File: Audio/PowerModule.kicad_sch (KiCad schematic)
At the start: 15 parts, among them J4 PWR_IN, J5 PWR_OUT, U1 TMR 6-1223

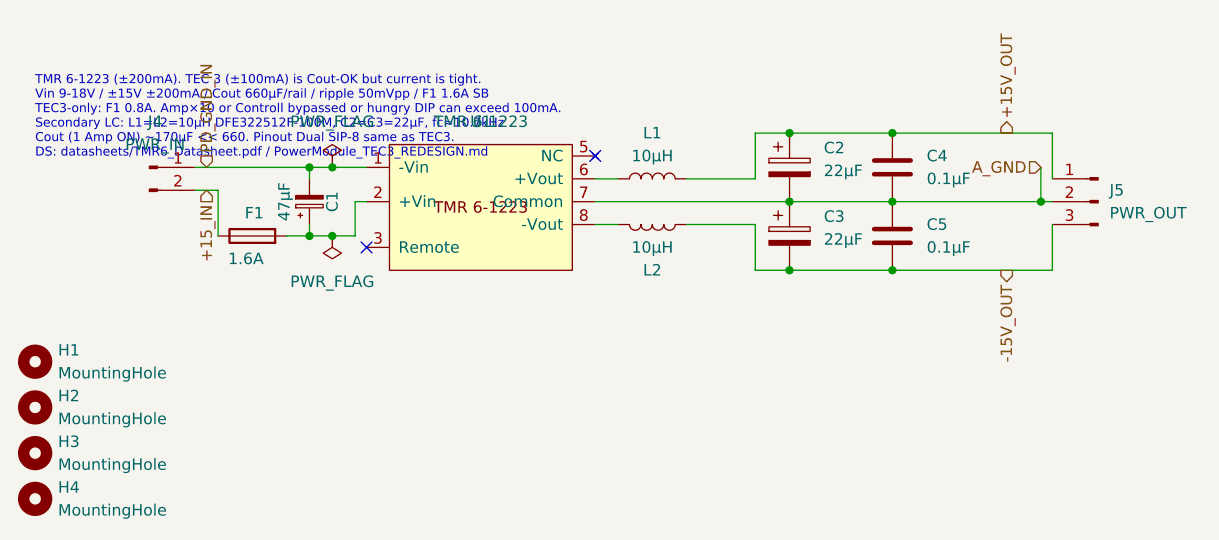
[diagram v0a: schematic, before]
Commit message: PowerModule の U1 を MEAN WELL DKMW20F-15 にする。
SIP-8 の TMR 6 では Amp 複数同時の電流が足りない。1インチ Dual に載せ替え、
ヒューズを 3A delay にし、ピン配置は SIP と別物としてシンボルと FP を新設する。

Co-authored-by: m_arino <indare@users.noreply.github.com>
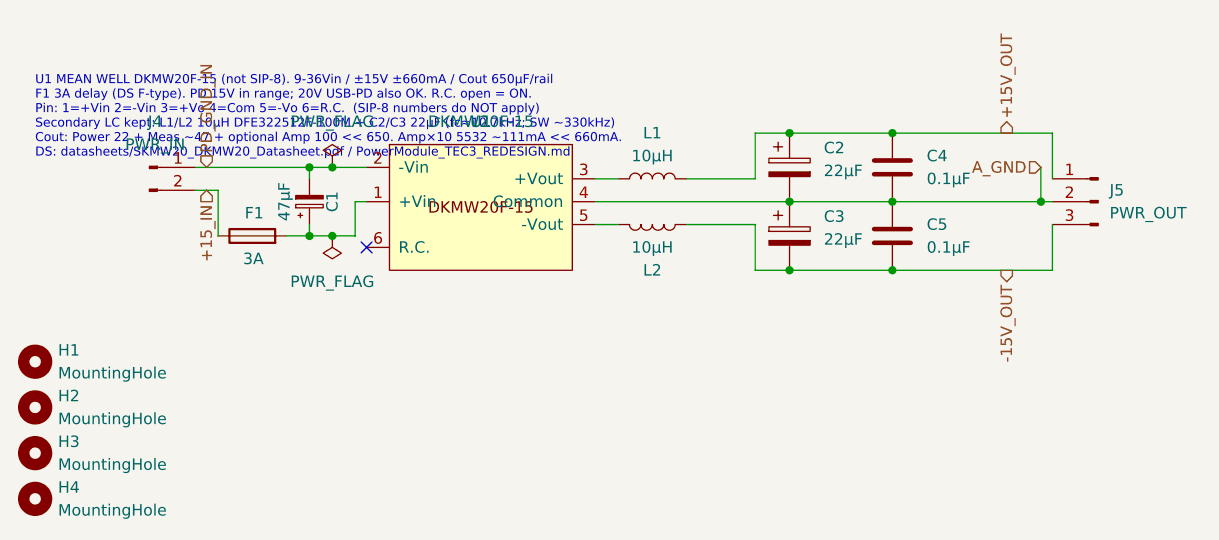
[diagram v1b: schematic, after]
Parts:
- F1: value 1.6A -> 3A
- U1: value TMR 6-1223 -> DKMW20F-15; footprint Library:TEC3-1223_SIP8_THT -> Library:DKMW20F-15_1in_THT; symbol TEC3:TEC3-1223 -> DKMW20:DKMW20F-15; MPN TMR 6-1223 -> DKMW20F-15; Manufacturer Traco Power -> MEAN WELL
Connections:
- net A_GND: now also U1.4 (Common); no longer U1.7 (Common)
- net PD_GND_IN: now also U1.2 (-Vin); no longer U1.1 (-Vin)
- net at L1.2: now also U1.3 (+Vout); no longer U1.6 (+Vout)
- net at C1.1, F1.2: now also U1.1 (+Vin); no longer U1.2 (+Vin)
- net at U1.5 (-Vout): now also L2.1
- no-connect marks 2 -> 1
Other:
- note added: "U1 MEAN WELL DKMW20F-15 (not SIP-8). 9-36Vin / ±15V ±660mA / Cout 650µF/rail F1 3A delay (DS F-type). PD 15V in range; 20V USB-PD also OK. R.C. open = ON. Pin: 1=+Vin 2=-Vin 3=+Vo 4=Com 5=-Vo 6=R.C. (SIP-8 numbers do NOT apply) Secondary LC kept: L1/L2 10µH DFE322512F-100M + C2/C3 22µF (fc≈10.7kHz; SW ~330kHz) Cout: Power 22 + Meas ~47 + optional Amp 100 << 650. Amp×10 5532 ~111mA << 660mA. DS: d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"
- note removed: "TMR 6-1223 (±200mA). TEC 3 (±100mA) is Cout-OK but current is tight. Vin 9-18V / ±15V ±200mA / Cout 660µF/rail / ripple 50mVpp / F1 1.6A SB TEC3-only: F1 0.8A. Amp×10 or Controll bypassed or hungry DIP can exceed 100mA. Secondary LC: L1=L2=10µH DFE322512F-100M, C2=C3=22µF, fc≈10.7kHz Cout (1 Amp ON) ~170µF << 660. Pinout Dual SIP-8 same as TEC3. DS: datasheets/TMR6_Datasheet.pdf / PowerModule_TEC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"
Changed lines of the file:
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@@
-	)
-	(no_connect
-		(at 77.47 35.56)
-		(uuid "b0a0tec3-0002-4000-8000-000000000002")
 	)
 	(no_connect
@@
 		)
 	)
-	(text "TMR 6-1223 (±200mA). TEC 3 (±100mA) is Cout-OK but current is tight.\nVin 9-18V / ±15V ±200mA / Cout 660µF/rail / ripple 50mVpp / F1 1.6A SB\nTEC3-only: F1 0.8A. Amp×10 or Controll bypassed or hungry DIP can exceed 100mA.\nSecondary LC: L1=L2=10µH DFE322512F-100M, C2=C3=22µF, fc≈10.7kHz\nCout (1 Amp ON) ~170µF << 660. Pinout Dual SIP-8 same as TEC3.\nDS: datasheets/TMR6_Datasheet.pdf / PowerModule_TEC3_REDESIGN.md"
+	(text "U1 MEAN WELL DKMW20F-15 (not SIP-8). 9-36Vin / ±15V ±660mA / Cout 650µF/rail\nF1 3A delay (DS F-type). PD 15V in range; 20V USB-PD also OK. R.C. open = ON.\nPin: 1=+Vin 2=-Vin 3=+Vo 4=Com 5=-Vo 6=R.C.  (SIP-8 numbers do NOT apply)\nSecondary LC kept: L1/L2 10µH DFE322512F-100M + C2/C3 22µF (fc≈10.7kHz; SW ~330kHz)\nCout: Power 22 + Meas ~47 + optional Amp 100 << 650. Amp×10 5532 ~111mA << 660mA.\nDS: datasheets/SKMW20_DKMW20_Datasheet.pdf / PowerModule_TEC3_REDESIGN.md"
 		(exclude_from_sim no)
 		(at 15.24 26.67 0)
@@
 			)
 		)
-		(property "Description" "12V input bulk after fuse. PCB: add Traco Class-A L=4.7uH + 10uF/4.7uF MLCC at U1 Vin"
+		(property "Description" "15V PD input bulk after fuse. PCB: keep Vin MLCC near U1; module is EMI Class A without extra parts"
 			(at 45.72 40.64 0)
 			(hide yes)
@@
 	)
 	(symbol
-		(lib_id "TEC3:TEC3-1223")
+		(lib_id "DKMW20:DKMW20F-15")
 		(at 64.77 31.75 0)
 		(unit 1)
@@
 			)
 		)
-		(property "Value" "TMR 6-1223"
+		(property "Value" "DKMW20F-15"
 			(at 64.77 31.75 0)
 			(show_name no)
@@
 			)
 		)
-		(property "Footprint" "Library:TEC3-1223_SIP8_THT"
+		(property "Footprint" "Library:DKMW20F-15_1in_THT"
 			(at 66.04 27.94 0)
 			(hide yes)
@@
 			)
 		)
-		(property "Datasheet" "https://www.tracopower.com/sites/default/files/products/datasheets/tmr6_datasheet.pdf"
+		(property "Datasheet" "https://www.meanwell.com/webapp/product/search.aspx?prod=DKMW20"
 			(at 65.278 29.972 0)
 			(hide yes)
@@
 			)
 		)
-		(property "Description" "Traco TMR 6-1223 ±15V/±200mA SIP-8; same Dual pinout as TEC 3-1223; DS: datasheets/TMR6_Datasheet.pdf"
+		(property "Description" "MEAN WELL DKMW20F-15 ±15V/±660mA 1in DIP; pinout NOT SIP-8; DS: datasheets/SKMW20_DKMW20_Datasheet.pdf"
 			(at 64.77 31.75 0)
 			(hide yes)
@@
 			)
 		)
-		(property "Manufacturer" "Traco Power"
+		(property "Manufacturer" "MEAN WELL"
 			(at 64.77 31.75 0)
 			(hide yes)
@@
 			)
 		)
-		(property "MPN" "TMR 6-1223"
+		(property "MPN" "DKMW20F-15"
 			(at 64.77 31.75 0)
 			(hide yes)
@@
 			)
 		)
+		(pin "6"
+		)
+		(pin "2"
+		)
+		(pin "1"
+		)
+		(pin "4"
+		)
+		(pin "5"
+		)
 		(pin "3"
-		)
-		(pin "1"
-		)
-		(pin "5"
-		)
-		(pin "7"
-		)
-		(pin "2"
-		)
-		(pin "8"
-		)
-		(pin "6"
 		)
 		(instances
@@
 			)
 		)
-		(property "Value" "1.6A"
+		(property "Value" "3A"
 			(at 40.64 46.99 90)
 			(show_name no)
@@
 			)
 		)
-		(property "Description" "Traco TMR 6-12xx recommended input fuse 1.6A slow-blow (TEC 3-12xx was 0.8A)"
+		(property "Description" "MEAN WELL DKMW20 F-type recommended input fuse 3A delay (slow-blow)"
 			(at 39.37 44.45 0)
 			(hide yes)
